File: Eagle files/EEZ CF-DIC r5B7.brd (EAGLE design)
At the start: 155 x 90 mm, 278 parts, among them IC1 VIPer35L, IC2 SI8233BB-D-IS1, IC3 LM5041B, IC4 LM258D, IC5 IR11688STRPBF, IC6 LM258D, IC7 TL103W, P1 T910W-50K, Q1 MMBT5551, Q10 BC856C, Q2 C3M0280090D, Q3 C3M0280090D, Q4 NYC0102BLT1G, Q5 IPW60R120P7, Q6 IPW60R120P7, Q7 FDD86250-F085, Q8 FDD86250-F085, Q9 BC856C, X1 39-30-3035, X2 22-05-7095, X3 B2B-ZR, X4 39-30-1020

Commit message: #4, #5, #6
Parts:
- removed D27: 1N5819HW-7-F, diode:SOD323-W
- removed D28: BAS316, EEZ_Lib1:SOD323-R
- removed SH4: (no value), EEZ_Lib1:SHORT_NOHOLE
- added C81: N.C., rcl:C0805
- added JP10: JP2-NOCUT, EEZ_Lib1:JP2-NOCUT
- added R100: 180K, rcl:R0805
- added R101, R103: 39K, rcl:R0805
- added R102: 18K, rcl:R0805
- added R99: 10K, rcl:R0805
- C14: value 1n/1kV -> 2n2/1kV
- C23: value 1500u -> 470u; device EEZ_Lib1:ECAP5/13 -> EEZ_Lib1:ECAP5/10.5
- C27: value 100p -> 47p
- C41, C63, C70: value 4n7/200V -> 4n7/500V
- C43: value 10n -> 100n
- C57: device EEZ_Lib1:ECAP7.5/18-H35.5-2A -> EEZ_Lib1:ECAP7.5/18-H35.5A
- C58: value N.C. -> 1u/100V; device EEZ_Lib1:ECAP7.5/18 -> rcl:C1206
- C59: value 1u/100V -> 47p/200V; device rcl:C1206 -> rcl:C0805
- C71: value 100n -> 47p/200V; device rcl:C0603 -> rcl:C0805
- C72: value 1n -> 100n; device rcl:C0805 -> rcl:C0603
- C73: value 100n -> 1n; device rcl:C0603 -> rcl:C0805
- C74: value 47p -> 100n; device rcl:C0805 -> rcl:C0603
- C75: value 100n -> 47p; device rcl:C0603 -> rcl:C0805
- C76: value 100p -> 100n; device rcl:C0805 -> rcl:C0603
- C77: value 470p -> 100p
- C78: value N.C. -> 470p; device EEZ_Lib1:EC1206 -> rcl:C0805
- C79: value 1u -> N.C.; device rcl:C0805 -> EEZ_Lib1:EC1206
- C80: value N.C. -> 1u
- D26: value 1N5819HW-7-F -> BAS316; device diode:SOD323-W -> EEZ_Lib1:SOD323-R
- D7: value 1N5819HW-7-F -> SS115; device diode:SOD323-W -> EEZ_Lib1:SMA
- JP3: value 0R-JUMPA -> JP2-NOCUT; device jump-0r-smd:A0R-JMP -> EEZ_Lib1:JP2-NOCUT
- JP4: value JP2-NOCUT -> 0R-JUMPA; device EEZ_Lib1:JP2-NOCUT -> jump-0r-smd:A0R-JMP
- JP6, JP9: value JP2-NOCUT -> JP3-CUT; device EEZ_Lib1:JP2-NOCUT -> EEZ_Lib1:JP3-CUT
- JP8: value JP3-CUT -> JP2-NOCUT; device EEZ_Lib1:JP3-CUT -> EEZ_Lib1:JP2-NOCUT
- R11: value 120R -> 36K; device rcl:R0805 -> rcl:R1206
- R12: value 100K -> 120R; device rcl:R1206 -> rcl:R0805
- R14: value 120R -> 100K; device rcl:R0805 -> rcl:R1206
- R15: value N.C. -> 120R
- R16, R38: value 47K -> N.C.
- R17: value 1K -> 16K
- R18: value 12K -> 1K
- R19: value 1K8 -> 4K7
- R20: value 47K -> 1K8
- R21: value 1K -> 47K
- R22: value 100K -> 1K; device rcl:R1206 -> rcl:R0805
- R23: value 10R -> 100K; device rcl:R0805 -> rcl:R1206
- R24: value 10K -> 10R
- R25: value 33R -> 10K
- R27: value 100K -> N.C.; device rcl:R1206 -> rcl:R0805
- R28: value 100R -> 100K; device rcl:R0805 -> rcl:R1206
- R30: value 22R/2-3W -> 100R; device rcl:R2512 -> rcl:R0805
- R31: value 100K -> 22R/2-3W; device rcl:R1206 -> rcl:R2512
- R32: value 22R/2-3W -> 86K6; device rcl:R2512 -> rcl:R1206
- R33: value 30K -> 22R/2-3W; device rcl:R0805 -> rcl:R2512
- R34: value 1R -> 30K
- R35: value 33R -> 1R
- R39: value 1R -> 47K
- R40: value 22R/2-3W -> 1R; device rcl:R2512 -> rcl:R0805
- R41: value 1K -> 22R/2-3W; device rcl:R0805 -> rcl:R2512
- R42: value 22R/2-3W -> 1K; device rcl:R2512 -> rcl:R0805
- R43, R72: value 10R -> N.C.; device rcl:R0805 -> rcl:R2512
- R44, R54: value 1K -> 10R
- R45: value 10R -> 1K
- R46: value 7K5 -> 10R
- R47: value 86K6 -> 8K2
- R49: value 10R -> 86K6
- R50: value 15K -> 10R
- R51: value 4K7 -> 15K
- R52: value 86K6 -> 4K7
- R53: value 10R -> 56K
- R55: value 6R2 -> 1K
- R56: value 1K -> 6R2
- R58: value 4K7 -> 1K
- R59: value 5K6 -> 4K7
- R6, R7: value N.C. -> 4K7
- R60: value 30K -> 5K6
- R61: value 1K -> 30K
- R62: value 30K -> 1K
- R63: value 10K -> 30K
- R64: value 1K -> 10K
- R66: value 120R -> 1K
- R67: value N.C. -> 120R; device rcl:R1210 -> rcl:R0805
- R69: value 22R/2-3W -> N.C.
- R70: value 3R3 -> N.C.; device rcl:R0805 -> rcl:R1210
- R71: value N.C. -> 1K; device rcl:R2512 -> rcl:R0805
- R73: value 47K -> 10R
- R74: value 3R3 -> 10R
- R75: value 22R/2-3W -> 100K; device rcl:R2512 -> rcl:R0805
- R76: value 22R/2-3W -> 10R; device rcl:R2512 -> rcl:R0805
- R77: value 10K -> 1K
- R78: value 470R -> 22R/2-3W; device rcl:R0805 -> rcl:R2512
- R79: value 470R -> N.C.; device rcl:R0805 -> rcl:R2512
- R8: value 100K -> 36K
- R80: value 150K -> 10K
- R81: value 10K -> 470R
- R82: value 1K -> 470R
- R83: value 30K -> 150K
- R84: value 1K8 -> 10K
- R86: value 86K6 -> 30K
- R88: value 3K3 -> 1K
- R89: value 1K -> 86K6
- R9: value 220K -> 100K
- R90: value 5K6 -> 1K8
- R91: value 7K5 -> 3K3
- R92: value 220R -> 1K
- R93: value 10K -> 5K6
- R94: value 10K -> 7K5
- R95: value 150K -> 220R
- R96: value 39K -> N.C.
- R97: value 15K -> N.C.
- R98: value 47K -> 10K
- TP5: device EEZ_connectors:TEST-PIN_1.2MM -> EEZ_connectors:TP_1.1MM_2
- TP6: device EEZ_connectors:TP_1.1MM_2 -> EEZ_Lib1:2MM-2
- ZD1: value BZX384-C15 -> BZX384-C13
- ZD4: value MMSZ5V1T1G -> BZT52C6V2; device EEZ_Lib1:SOD323-W -> EEZ_Lib1:SOD123
- moved R79 99.0 mm to (43.6, 9.65), turned to 270 degrees
- moved TP5 98.1 mm to (141.2, 4.13), turned to 180 degrees
- moved R78 95.3 mm to (47.5, 9.65), turned to 270 degrees
- moved D26 82.0 mm to (141.9, 14.0), turned to 0 degrees
- moved TP6 81.5 mm to (59.8, 6.73), turned to 90 degrees
- moved R41 80.9 mm to (13.0, 64.5)
- moved R42 77.2 mm to (88.7, 35.9)
- moved R71 75.8 mm to (54.8, 22.5), turned to 180 degrees
- moved R82 71.8 mm to (142.0, 16.1), flipped to the top, turned to 0 degrees
- moved EEZ_SIGNATURE 69.4 mm to (60.0, 34.3)
- moved R72 66.5 mm to (128.9, 6.35), flipped to the top, turned to 270 degrees
- moved R31 65.6 mm to (13.9, 26.0), flipped to the bottom, turned to 0 degrees
- moved R70 63.7 mm to (123.5, 4.89), flipped to the bottom, turned to 270 degrees
- moved R81 62.8 mm to (142.0, 18.0), turned to 0 degrees
- moved JP3 60.3 mm to (110.8, 67.7), turned to 180 degrees
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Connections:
- removed net +14V: C29.2, C30.2, C52.1, C53.1, IC4.8, JP1.2, OK2.1, R23.2, R36.2, R45.2
- removed net N$67 (its old number): C70.1, R75.2, R76.2
- removed net N$74: D26.C, IC5.1, R70.2
- removed net N$75: D27.C, IC5.8, R74.2
- removed net S1_OUT: SH3.P$1, TR3.S1
- removed net S2_DOT_OUT: SH4.P$2, TR3.S2_DOT
- removed net SR_OUT1: D26.A, Q7.1, R70.1
- removed net SR_OUT2: D27.A, Q8.1, R74.1
- new net +12V: C29.2, C30.2, C52.1, C53.1, IC4.8, JP1.2, OK2.1, R24.2, R37.2, R46.2
- new net G1_OUT: Q7.1, R73.1
- new net G2_OUT: Q8.1, R76.1
- new net GATE1: IC5.1, R73.2
- new net GATE2: IC5.8, R76.2
- new net N$66: C70.1, R78.2, R79.2
- new net N$71: C73.1, JP6.COM
- new net N$73: R96.1, R97.2
- new net N$77: R97.1, TP6.1
- new net N$78: R11.2, R8.2
- new net S_COMM: JP6.NC, SH3.P$1, TR3.S1, TR3.S2_DOT
- new net VD1: C59.2, IC5.4, R71.1
- new net VD2: C71.2, IC5.5, R77.2
- net !FAULT: now also D26.C; no longer D28.C
- net +2.5VREF: now also C80.1, R84.2, R90.1; no longer C79.1, R81.2, R87.1
- net +5VREF: now also R100.1, R44.1, R60.2, R98.1; no longer R43.1, R58.2, R93.1, R95.1
- net +6V_REC: now also R15.1, R18.1; no longer R14.1, R17.1
- net -7V_REC: now also R12.1; no longer R11.1
- net 0V: now also R19.1, R21.2, R40.1, R40.2; no longer R18.1, R19.2, R38.2, R39.1, TP5.1
- net 12V_COMM: now also JP4.2; no longer JP3.2
- net AGND: now also R102.2, R35.1, R35.2, R47.2, R51.2, R53.2, R58.2, R66.2, R99.2; no longer R33.1, R34.2, R46.2, R50.2, R52.2, R56.2, R61.2, R94.2, R97.2
- net AUX_AC: now also R16.2; no longer R15.2
- net CLAMP_C: now also R41.1, R43.1, R49.2; no longer R40.1, R42.1, R48.2
- net COMP: now also JP10.1; no longer JP9.1
- net CT_OUT+: now also R25.1; no longer R24.1
- net CT_OUT-: now also R25.2, R56.2, R58.1; no longer R24.2, R55.2, R57.1
- net DC_BUS: now also JP3.1, R23.1; no longer JP4.1, R22.1
- net FB: now also R48.1, R57.1, R61.1; no longer R47.1, R56.1, R60.1
- net FB2: now also R22.1; no longer R21.1
- net GND: now also C58.2, C59.1, C71.1, C72.2, C74.2, C76.2, C79.-, C81.2, JP4.3, R72.1, R75.2, TP5.GND, TP6.2; no longer C58.-, C59.2, C71.2, C73.2, C75.2, C78.-, C79.2, JP3.3, R71.1, R73.2, TP6.GND
- net HD: now also R29.2; no longer R28.2
- net HI_OUT: now also R27.2; no longer R25.2
- net LD: now also R30.2; no longer R29.2
- net LO_OUT: now also R36.1, R38.1; no longer R35.1, R37.1
- net L_PUSH: now also R31.2; no longer R30.2
- net N$1: now also D26.A; no longer D28.A
- net N$10: now also C75.2, R89.1, R93.1; no longer C74.2, R86.1, R90.1
- net N$100: now also R52.1; no longer R51.1
- net N$11: now also R82.2; no longer R79.2
- net N$12: now also R83.1, R87.2; no longer R80.1, R84.2
- net N$13: now also R50.1; no longer R49.1
- net N$130: now also R42.2; no longer R41.2
- net N$132: now also R80.2, R84.1; no longer R77.2, R81.1
- net N$134: now also C77.1, R95.2; no longer C76.1, R92.2
- net N$135: now also R18.2; no longer R17.2
- net N$137: now also R11.1; no longer R9.2
- net N$14: now also R54.1; no longer R53.1
- net N$141: now also R17.1, R19.2; no longer R15.1, R18.2
- net N$144: now also R12.2; no longer R11.2
- net N$146: now also R15.2; no longer R14.2
- net N$152: now also R21.1; no longer R20.1
- net N$155: now also R17.2; no longer R16.2
- net N$16: now also R81.2; no longer R78.2
- net N$17: now also R33.1; no longer R32.1
- net N$18: now also R75.1; no longer R73.1
- net N$19: now also R53.1; no longer R52.1
- net N$2: now also R28.2, R32.1; no longer R27.2, R31.1
- net N$20: now also R14.2, R20.1; no longer R13.2, R19.1
- net N$21: now also R26.1; no longer R25.1
- net N$22: now also R51.1; no longer R50.1
- net N$25: now also R45.1; no longer R44.1
- net N$26: now also R59.1, R63.1; no longer R58.1, R62.1
- net N$28: now also C73.2, R86.2; no longer C72.2, R83.2
- net N$29: now also R36.2, R39.1; no longer R35.2, R38.1
- net N$30: now also R48.2, R49.1; no longer R47.2, R48.1
- net N$31: now also R24.1; no longer R23.1
- net N$32: now also R42.1; no longer R41.1
- net N$34: now also R61.2; no longer R60.2
- net N$35: now also R41.2, R43.2; no longer R40.2, R42.2
- net N$36: now also R29.1; no longer R28.1
- net N$37: now also R55.2; no longer R54.2
- net N$39: now also C76.1, JP8.1; no longer C75.1, JP7.1
- net N$40: now also R30.1; no longer R29.1
- net N$42: now also R64.1; no longer R63.1
- net N$44: now also JP10.2; no longer JP9.2
- net N$45: now also R27.1; no longer R26.1
- net N$46: now also C72.1, C74.1, JP7.2, R74.1, R90.2, R91.2; no longer C71.1, C73.1, JP6.2, R72.1, R87.2, R88.2
- net N$48: now also R34.2; no longer R33.2
- net N$49: now also R13.2, R14.1; no longer R12.2, R13.1
- net N$5: now also R31.1, R33.2; no longer R30.1, R32.2
- net N$50: now also R86.1, R87.1, R93.2, R94.2, R96.2; no longer R83.1, R84.1, R90.2, R91.2
- net N$51: now also R52.2, R62.1; no longer R51.2, R61.1
- net N$52: now also R38.2; no longer R37.2
- net N$53: now also R80.1, R85.2; no longer R77.1, R82.2
- net N$54: now also R46.1; no longer R45.1
- net N$56: now also R56.1; no longer R54.1
- net N$57: now also C81.1, JP9.COM; no longer C80.1, JP8.COM
- net N$58: now also JP9.NO; no longer JP8.NO
- net N$59: now also R66.1; no longer R65.1
- net N$6: now also R23.2, R28.1; no longer R22.2, R27.1
- net N$60: now also R13.1, R9.2; no longer R12.1, R8.2
- net N$61: now also R99.1; no longer R94.1
- net N$62: now also R98.2; no longer R93.2
- net N$63: now also R37.1; no longer R36.1
- net N$64: now also C77.2, R85.1, R88.2, R92.1; no longer C76.2, R82.1, R85.2, R89.1
- net N$68: now also R101.2, R102.1, R103.1; no longer R96.2, R97.1, R98.1
- net N$7: now also R60.1, R65.1; no longer R59.1, R64.1
- net N$70: now also R100.2, R101.1; no longer R95.2, R96.1
- net N$76: now also C75.1, C78.1; no longer C74.1, C77.1
- net N$8: now also R70.1; no longer R67.1
- net N$9: now also C78.2, R89.2; no longer C77.2, R86.2
- net NFB_OFFSET: now also C79.+, R88.1, R94.1, R95.1; no longer C78.+, R85.1, R91.1, R92.1
- net OK_A: now also R91.1; no longer R88.1
- net POUT+: now also C58.1, R67.1; no longer C58.+, C59.1, R66.1, SH4.P$1
- net PREG_OUT+: now also JP4.1, JP6.NO, R70.2, R72.2, R83.2, TP5.TIP; no longer C72.1, JP3.1, R66.2, R71.2, R80.2, TP6.TIP
- net PULL: now also R54.2; no longer R53.2
- net PUSH: now also R50.2; no longer R49.2
- net REF: now also R44.2; no longer R43.2
- net S1_DOT_OUT: now also Q8.3, R77.1, R78.1, R79.1; no longer IC5.4, Q7.3, R68.1, R69.1
- net S2_OUT: now also Q7.3, R68.1, R69.1, R71.2; no longer IC5.5, Q8.3, R75.1, R76.1
- net SYNC_VCC: now also R74.2; no longer R72.2
- net UVLO: now also R103.2, R32.2, R45.2, R47.1; no longer R31.2, R44.2, R46.1, R98.2
- net U_CTRL: now also JP9.NC; no longer JP8.NC
- net U_MON1: now also R92.2; no longer R89.2
- net V+: now also JP7.1, R22.2, R81.1, R82.1; no longer JP6.1, R21.2, R78.1, R79.1
- net V-: now also JP8.2; no longer JP7.2
- net VIPER+: now also JP3.2; no longer JP4.2
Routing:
- net +14V: track 108.3 -> 0.00 mm, vias 6 -> 0
- net +12V: track 0.00 -> 107.7 mm, vias 0 -> 6
- net S_COMM: track 0.00 -> 62.7 mm
- net S2_DOT_OUT: track 39.2 -> 0.00 mm
- net POUT+: track 12.8 -> 38.9 mm, vias 2 -> 1
- net S1_OUT: track 24.4 -> 0.00 mm
- net N$1: track 13.5 -> 29.9 mm
- net S2_OUT: track 40.3 -> 26.0 mm, vias 25 -> 27
- net S1_DOT_OUT: track 22.4 -> 10.8 mm, vias 18 -> 27
- net 0V: track 701.4 -> 690.7 mm, vias 22 -> 23
- net N$77: track 0.00 -> 9.72 mm
- net PREG_OUT+: track 58.6 -> 68.2 mm
- net N$66: track 0.00 -> 7.80 mm
- net SR_OUT2: track 7.50 -> 0.00 mm, vias 1 -> 0
- net N$46: track 55.1 -> 47.6 mm, vias 3 -> 2
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- added copper zone on layer 16, net G1_OUT
- added copper zone on layer 16, net G2_OUT
- removed copper zone on layer 16, net SR_OUT1
- removed copper zone on layer 16, net SR_OUT2
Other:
- board text added: "EEZ CF-DIC (03/2019 r5B7)"
- board text removed: "EEZ CF-DIC (01/2019 r5B6)"
- board text removed: "Okrenuti C57 !!!"
- board text removed: "R41 povecati na 1K8?"

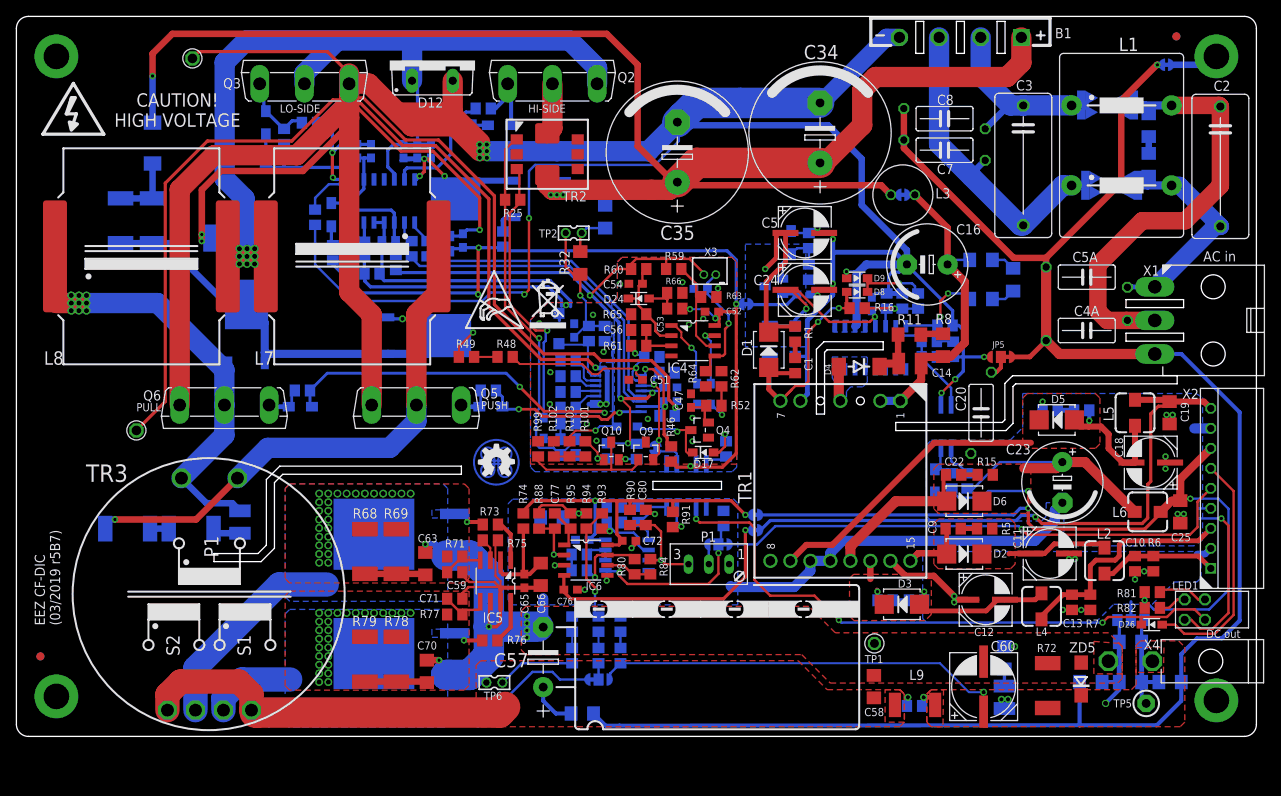
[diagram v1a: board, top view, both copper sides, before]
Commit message: changed SR mosfets package
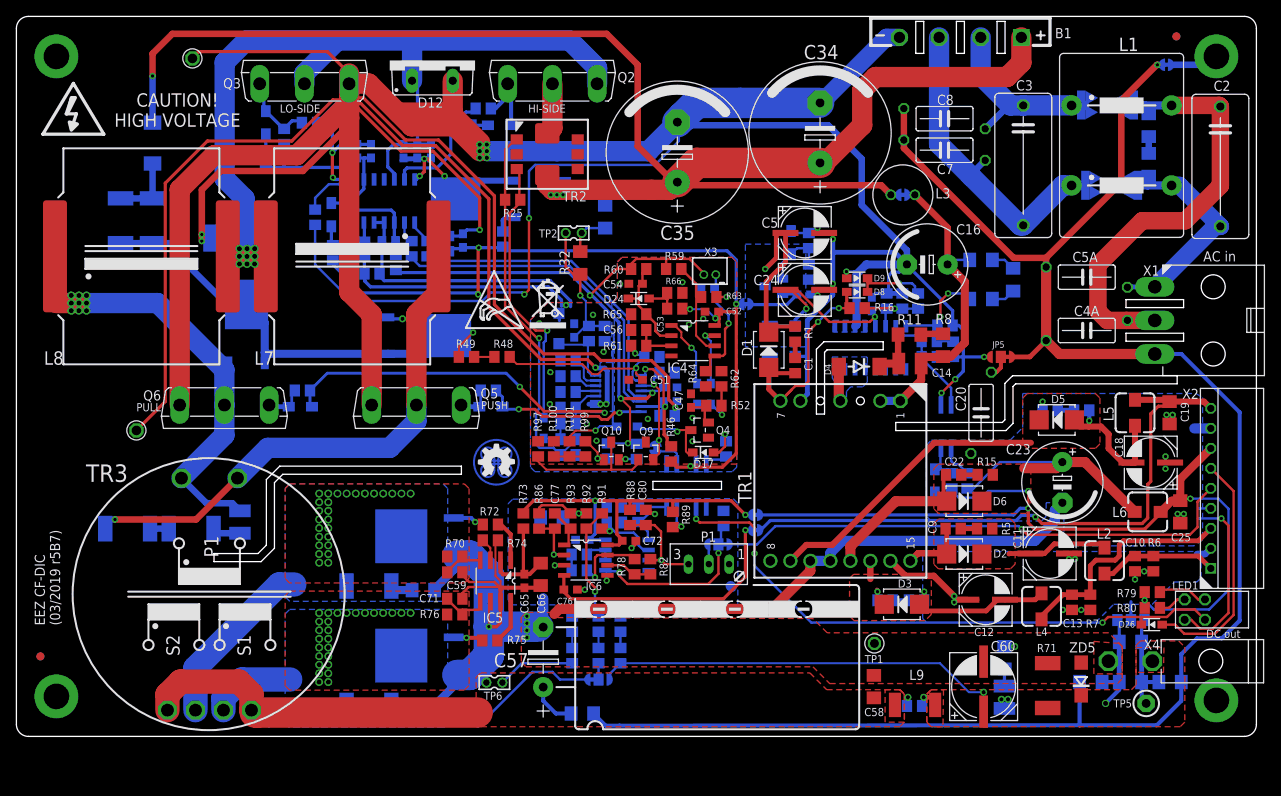
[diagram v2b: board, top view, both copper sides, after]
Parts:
- removed R102: 18K, rcl:R0805
- removed R103: 39K, rcl:R0805
- D7: value SS115 -> SS100B
- Q7, Q8: device EEZ_Lib1:TO263 -> EEZ_Lib1:TO229P990X239-3N
- R100: value 180K -> 18K
- R61: value 30K -> 86K6
- R69: device rcl:R2512 -> rcl:R1210
- R70: value N.C. -> 1K; device rcl:R1210 -> rcl:R0805
- R71: value 1K -> N.C.; device rcl:R0805 -> rcl:R2512
- R72: value N.C. -> 10R; device rcl:R2512 -> rcl:R0805
- R74: value 10R -> 100K
- R75: value 100K -> 10R
- R76: value 10R -> 1K
- R77: value 1K -> 22R/2-3W; device rcl:R0805 -> rcl:R2512
- R78: value 22R/2-3W -> 10K; device rcl:R2512 -> rcl:R0805
- R79: value N.C. -> 470R; device rcl:R2512 -> rcl:R0805
- R80: value 10K -> 470R
- R81: value 470R -> 150K
- R82: value 470R -> 10K
- R83: value 150K -> 1K
- R84: value 10K -> 30K
- R85, R88: value 1K -> 1K8
- R86: value 30K -> 1K
- R87: value 1K8 -> 86K6
- R89: value 86K6 -> 3K3
- R90: value 1K8 -> 1K
- R91: value 3K3 -> 5K6
- R92: value 1K -> 7K5
- R93: value 5K6 -> 220R
- R94: value 7K5 -> N.C.
- R95: value 220R -> N.C.
- R96, R97: value N.C. -> 10K
- R98: value 10K -> 180K
- R99: value 10K -> 39K
- moved R79 98.8 mm to (142.0, 18.0), turned to 0 degrees
- moved R69 78.2 mm to (123.5, 4.89), flipped to the bottom
- moved R71 75.8 mm to (128.9, 6.35), turned to 270 degrees
- moved R72 72.5 mm to (59.2, 26.5), turned to 0 degrees
- moved R70 70.9 mm to (54.8, 22.5), flipped to the top, turned to 180 degrees
- moved R81 67.0 mm to (75.5, 10.1), flipped to the bottom, turned to 270 degrees
- moved R80 64.9 mm to (142.0, 16.1), turned to 0 degrees
- moved R82 62.9 mm to (79.2, 21.2), turned to 90 degrees
- moved R78 31.9 mm to (77.3, 21.2)
- moved R97 26.2 mm to (65.2, 35.9), flipped to the top
- moved R96 23.0 mm to (77.5, 35.6), turned to 270 degrees
- moved R95 16.8 mm to (69.5, 10.1), flipped to the bottom, turned to 90 degrees
- moved R77 15.6 mm to (44.1, 3.87), flipped to the bottom, turned to 180 degrees
- moved R86 14.9 mm to (65.3, 26.9), flipped to the top
- moved R87 14.7 mm to (74.7, 28.7), turned to 180 degrees
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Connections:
- net +2.5VREF: now also R82.2, R88.1; no longer R84.2, R90.1
- net +5VREF: now also R96.1; no longer R100.1
- net AGND: now also R100.2, R97.2; no longer R102.2, R99.2
- net G1_OUT: now also R72.1; no longer R73.1
- net G2_OUT: now also R75.1; no longer R76.1
- net GATE1: now also R72.2; no longer R73.2
- net GATE2: now also R75.2; no longer R76.2
- net GND: now also Q7.3, Q8.3, R71.1, R74.2; no longer Q7.2, Q8.2, R72.1, R75.2
- net N$10: now also R87.1, R91.1; no longer R89.1, R93.1
- net N$11: now also R80.2; no longer R82.2
- net N$12: now also R81.1, R85.2; no longer R83.1, R87.2
- net N$132: now also R78.2, R82.1; no longer R80.2, R84.1
- net N$134: now also R93.2; no longer R95.2
- net N$16: now also R79.2; no longer R81.2
- net N$18: now also R74.1; no longer R75.1
- net N$28: now also R84.2; no longer R86.2
- net N$46: now also R73.1, R88.2, R89.2; no longer R74.1, R90.2, R91.2
- net N$50: now also R84.1, R85.1, R91.2, R92.2; no longer R86.1, R87.1, R93.2, R96.2
- net N$53: now also R78.1, R83.2; no longer R80.1, R85.2
- net N$61: now also R97.1; no longer R99.1
- net N$62: now also R96.2; no longer R98.2
- net N$64: now also R83.1, R86.2, R90.1; no longer R85.1, R88.2, R92.1
- net N$66: now also R77.2; no longer R78.2, R79.2
- net N$67: no longer R69.2
- net N$68: now also R100.1, R101.1, R99.2; no longer R101.2, R102.1, R103.1
- net N$70: now also R98.2, R99.1; no longer R100.2, R101.1
- net N$73: now also R94.1, R95.2; no longer R96.1, R97.2
- net N$77: now also R95.1; no longer R97.1
- net N$8: now also R69.1; no longer R70.1
- net N$9: now also R87.2; no longer R89.2
- net NFB_OFFSET: now also R86.1, R92.1, R93.1; no longer R88.1, R94.1, R95.1
- net OK_A: now also R89.1; no longer R91.1
- net PREG_OUT+: now also R69.2, R71.2, R81.2; no longer R70.2, R72.2, R83.2
- net S1_DOT_OUT: now also Q8.2, R76.1; no longer Q8.3, R78.1, R79.1
- net S2_OUT: now also Q7.2, R70.2; no longer Q7.3, R69.1, R71.2
- net SYNC_VCC: now also R73.2; no longer R74.2
- net UVLO: now also R101.2; no longer R103.2
- net U_MON1: now also R90.2; no longer R92.2
- net V+: now also R79.1, R80.1; no longer R81.1, R82.1
- net VD1: now also R70.1; no longer R71.1
- net VD2: now also R76.2; no longer R77.2
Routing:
- net GND: track 178.0 -> 201.3 mm, vias 20 -> 18
- net N$66: track 7.80 -> 2.80 mm
- net N$67: track 7.57 -> 2.80 mm
- net S2_OUT: track 26.0 -> 21.9 mm
- net POUT+: track 38.9 -> 35.1 mm
- net !FAULT: track 76.5 -> 75.4 mm
- net N$42: track 16.1 -> 15.3 mm
- net G2_OUT: track 4.32 -> 3.73 mm
- net G1_OUT: track 4.63 -> 4.04 mm
- removed copper zone on layer 16, net G1_OUT
- removed copper zone on layer 16, net G2_OUT

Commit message: r5B7 BOM
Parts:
- C27, C75: value 47p -> 47p/200V
- C41: value 4n7/500V -> 2n2/1kV
- C57: value UPW1J152MHD -> UVZ1J222MHD
- C63, C70: value 4n7/500V -> 2n2/1kV; device rcl:C1206 -> rcl:C1210
- D11, D14: value 1N5819HW-7-F -> N.C.
- Q5, Q6: value IPW60R120P7 -> IRFP4332PBF
- R32: device rcl:R1206 -> rcl:R0805
- R70, R76: value 1K -> 1K8
- R74: value 100K -> 86K6
- ZD1: value BZX384-C13 -> BZT52C13; device EEZ_Lib1:SOD323-W -> EEZ_Lib1:SOD123
- ZD3: device EEZ_Lib1:SOD323-W -> EEZ_Lib1:SOD123
- moved ZD3 0.45 mm to (114.9, 31.5)
- moved ZD1 0.39 mm to (96.8, 61.3)
- moved R18 0.25 mm to (119.1, 31.9)
- moved R22 0.25 mm to (117.2, 31.9)
- moved C63 0.14 mm to (50.8, 18.4)
- moved C70 0.13 mm to (50.9, 3.49)
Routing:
- net S_COMM: track 62.7 -> 73.1 mm, vias 0 -> 1
- net AUX_REC: track 24.8 -> 21.4 mm
- net V+: track 108.3 -> 107.5 mm
- net N$133: track 8.07 -> 7.33 mm
